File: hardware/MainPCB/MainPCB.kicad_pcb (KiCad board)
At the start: 2 copper layers, 150 x 60 mm, 34 parts, among them J1 USB4125-GF-A, SW1 SW_Push, U1 ESP32-CAM, U2 LSM6DSO32XTR, U3 RASPBERRY_PI_PICO, U4 TIP120

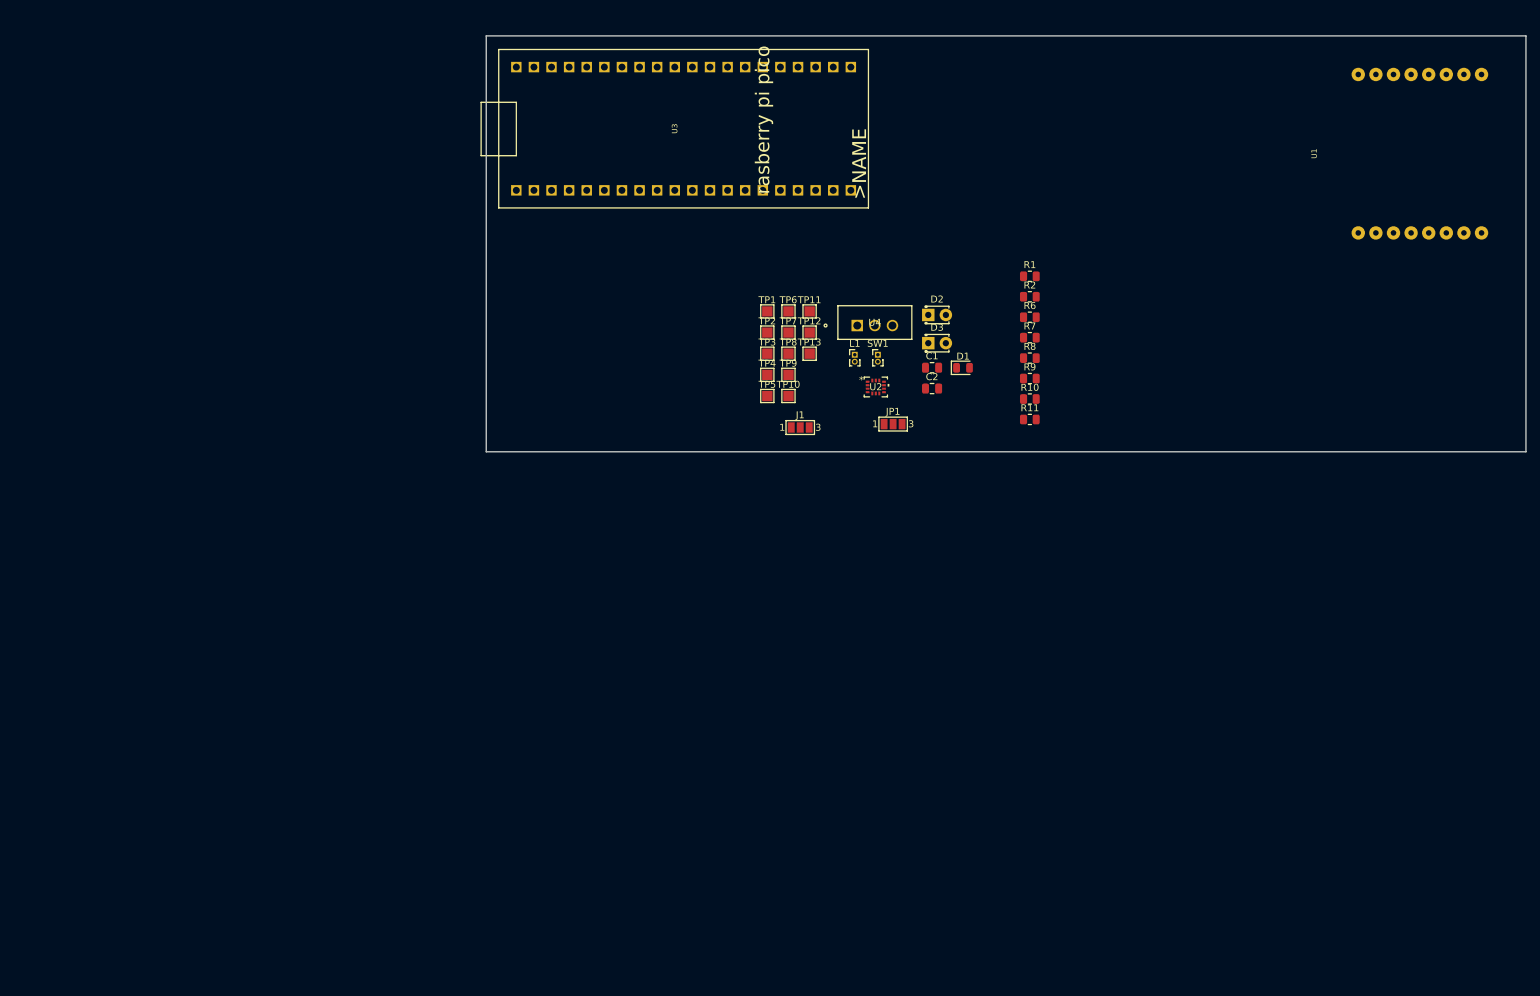
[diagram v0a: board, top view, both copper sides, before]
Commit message: fix: Fixed the LED_GND connecting to GND, also swapped rx and tx on esp32
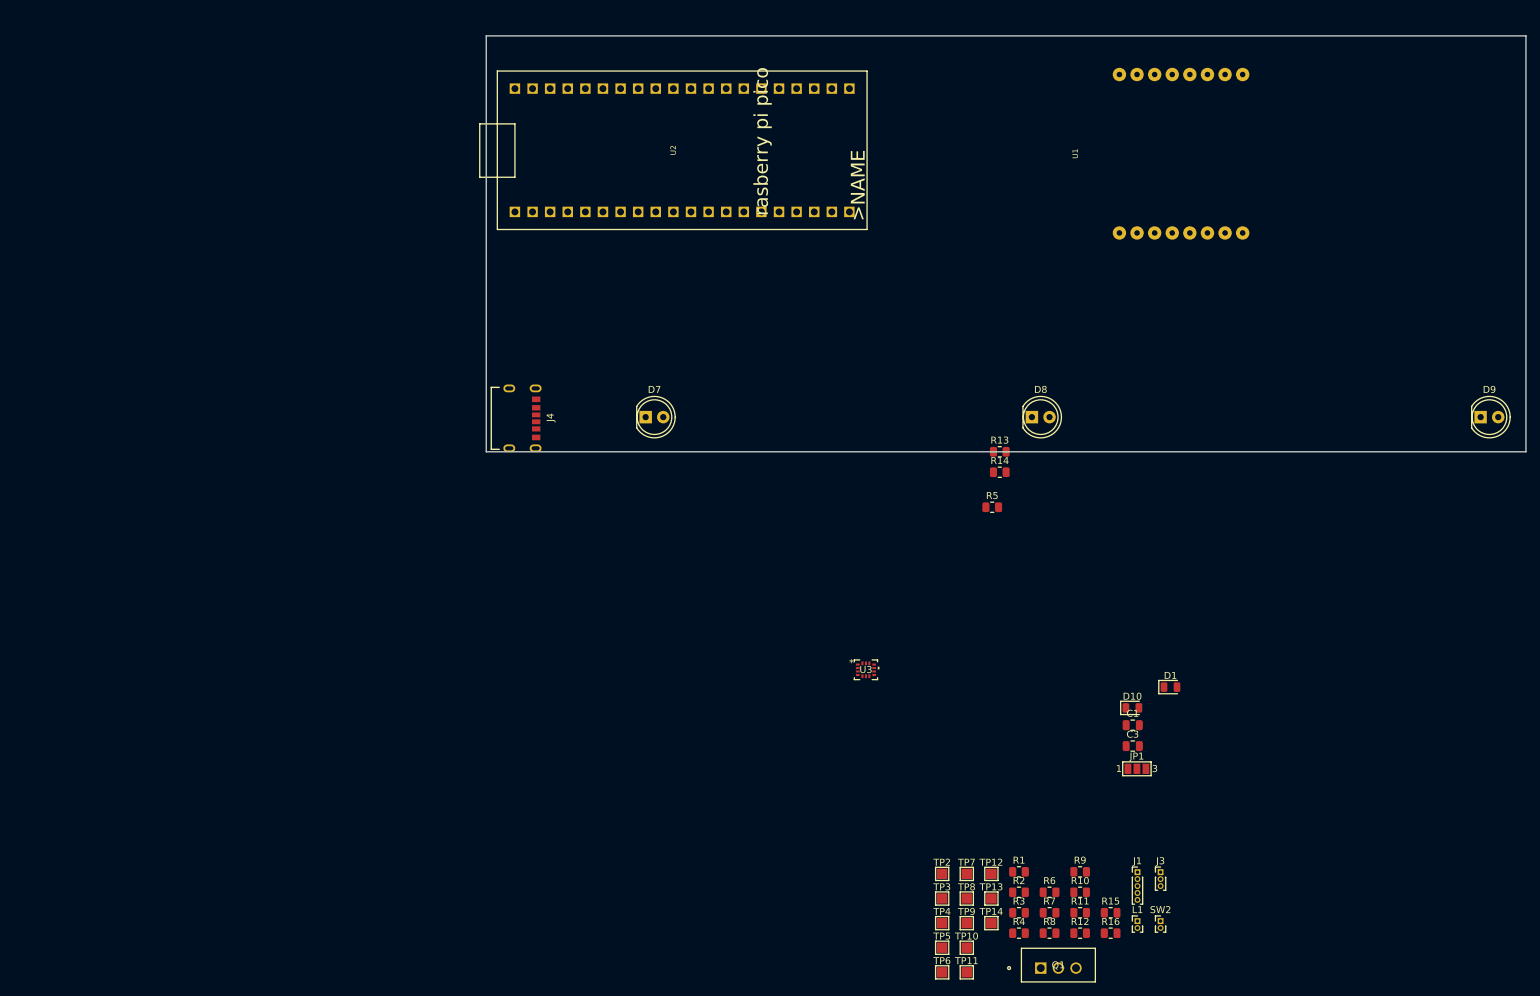
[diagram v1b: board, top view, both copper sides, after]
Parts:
- removed C2: 100nF, Capacitor_SMD:C_0805_2012Metric
- removed D2, D3: Diode, LED_THT:LED_D1.8mm_W3.3mm_H2.4mm
- removed SW1: SW_Push, Connector_PinHeader_1.00mm:PinHeader_1x02_P1.00mm_Vertical
- removed TP1: TestPoint, TestPoint:TestPoint_Pad_1.5x1.5mm
- removed U4: TIP120, Footprints:TO-220_STM
- added C3: 100nF, Capacitor_SMD:C_0805_2012Metric, F.Cu at (143.3, 152.5)
- added D10: Switch Status LED, LED_SMD:LED_0805_2012Metric, F.Cu at (143.2, 146.9)
- added D7: IR LED, LED_THT:LED_D5.0mm, F.Cu at (73.0, 105.0)
- added D8: IR LED, LED_THT:LED_D5.0mm, F.Cu at (128.7, 105.0)
- added D9: IR LED, LED_THT:LED_D5.0mm, F.Cu at (193.5, 105.0)
- added J3: Conn_01x03, Connector_PinHeader_1.00mm:PinHeader_1x03_P1.00mm_Vertical, F.Cu at (147.3, 170.7)
- added J4: USB4125-GF-A_REVA2, Footprints:GCT_USB4125-GF-A_REVA2, F.Cu at (54.1, 105.2)
- added Q1: TIP120, Footprints:TO-220_STM, F.Cu at (130.0, 184.5)
- added R12: 0, Resistor_SMD:R_0805_2012Metric, F.Cu at (135.7, 179.4)
- added R13: 220, Resistor_SMD:R_0805_2012Metric, F.Cu at (124.1, 110.0)
- added R14: 220, Resistor_SMD:R_0805_2012Metric, F.Cu at (124.1, 113.0)
- added R15: 0, Resistor_SMD:R_0805_2012Metric, F.Cu at (140.1, 176.5)
- added R16: 0, Resistor_SMD:R_0805_2012Metric, F.Cu at (140.1, 179.4)
- added R3: 1k, Resistor_SMD:R_0805_2012Metric, F.Cu at (126.9, 176.5)
- added R4: 5.1k, Resistor_SMD:R_0805_2012Metric, F.Cu at (126.9, 179.4)
- added R5: 220, Resistor_SMD:R_0805_2012Metric, F.Cu at (123.0, 118.0)
- added SW2: SW_Push, Connector_PinHeader_1.00mm:PinHeader_1x02_P1.00mm_Vertical, F.Cu at (147.3, 177.7)
- added TP14: Switch_TP, TestPoint:TestPoint_Pad_1.5x1.5mm, F.Cu at (122.9, 178.0)
- D1: value Diode -> 1N4004
- J1: value USB4125-GF-A -> Conn_01x05; footprint Jumper:SolderJumper-3_P1.3mm_Open_Pad1.0x1.5mm_NumberLabels -> Connector_PinHeader_1.00mm:PinHeader_1x05_P1.00mm_Vertical
- L1: value L -> Solenoid
- R10: value 0 -> 1k
- R2: value 1k -> 5.1k
- TP10: value TestPoint -> VUSB_TP
- TP11: value TestPoint -> GND_TP
- TP12: value TestPoint -> 3V3_TP
- TP13: value TestPoint -> MOSI_TP
- TP2: value TestPoint -> Transistor_Base_TP
- TP3: value TestPoint -> Transistor_GND_TP
- TP4: value TestPoint -> MISO_TP
- TP5: value TestPoint -> SDA_TP
- TP6: value TestPoint -> SCL_TP
- TP7: value TestPoint -> CS1_TP
- TP8: value TestPoint -> CS2_TP
- TP9: value TestPoint -> SCK_TP
- U2: value LSM6DSO32XTR -> RASPBERRY_PI_PICO; footprint Footprints:LGA_O32XTR_STM -> Footprints:RASPBERRY_PI_PICO
- U3: value RASPBERRY_PI_PICO -> LSM6DSO32XTR; footprint Footprints:RASPBERRY_PI_PICO -> Footprints:LGA_O32XTR_STM
- moved TP11 98.0 mm to (119.3, 185.1)
- moved TP6 97.9 mm to (115.8, 185.1)
- moved L1 91.3 mm to (144.0, 177.7)
- moved R2 85.9 mm to (126.9, 173.6)
- moved R1 85.9 mm to (126.9, 170.6)
- moved TP10 83.7 mm to (119.3, 181.6)
- moved TP5 83.5 mm to (115.8, 181.6)
- moved TP9 83.2 mm to (119.3, 178.0)
- moved TP4 83.0 mm to (115.8, 178.0)
- moved R6 83.0 mm to (131.3, 173.6)
- moved R7 83.0 mm to (131.3, 176.5)
- moved R8 83.0 mm to (131.3, 179.4)
- moved TP13 82.9 mm to (122.9, 174.4)
- moved U3 82.8 mm to (104.8, 141.4), turned to 0 degrees
- moved TP8 82.7 mm to (119.3, 174.4)
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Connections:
- C1 pad 1: +5V -> 3V3
- C1 pad 2: Net-(U2-Vdd_IO) -> GND
- D1 pad 2: +5V -> VUSB
- J1 pad 1: (no net) -> /PI_IO12
- J1 pad 2: (no net) -> /PI_IO13
- J1 pad 3: (no net) -> /PI_IO13
- L1 pad 2: +5V -> VUSB
- R1 pad 2: Net-(R1-Pad2) -> Net-(Q1-Pad1)
- R10 pad 2: +5V -> GND
- R11 pad 1: Net-(D3-A) -> Net-(R11-Pad1)
- R11 pad 2: +5V -> /CS2
- R2 pad 1: /Switch -> Net-(J4-CC2)
- R2 pad 2: +5V -> GND_LED
- R6 pad 1: Net-(R6-Pad1) -> Net-(U3-SDA)
- R6 pad 2: /SCL -> /SDA
- R7 pad 1: /MOSI -> Net-(U3-SDA)
- R7 pad 2: Net-(U2-SDA) -> /MOSI
- R8 pad 1: /SCL -> Net-(U3-SCL)
- R8 pad 2: Net-(U2-SCL) -> /SCL
- R9 pad 1: /MOSI -> Net-(U3-SCL)
- R9 pad 2: Net-(R9-Pad2) -> /SCK
- TP10 pad 1: /MISO -> VUSB
- TP11 pad 1: /CS1 -> GND
- TP12 pad 1: /MOSI -> 3V3
- TP13 pad 1: /SCL -> /MOSI
- TP2 pad 1: Net-(JP1-C) -> Net-(Q1-Pad1)
- TP4 pad 1: /Switch -> /MISO
- TP5 pad 1: /CS2 -> /SDA
- TP6 pad 1: /MISO -> /SCL
- TP7 pad 1: /Solenoid -> /CS1
- TP8 pad 1: /SCK -> /CS2
- TP9 pad 1: /MOSI -> /SCK
- U1 pad 5V: unconnected-(U1-Pad5V) -> VUSB
- U1 pad IO12: /MISO -> Net-(R15-Pad1)
- U1 pad IO13: /CS2 -> Net-(R11-Pad1)
- U1 pad IO16: Net-(R6-Pad1) -> /SCL
- U1 pad IO2: unconnected-(U1-PadIO2) -> /CAM_IO2
- U1 pad IO4: Net-(R9-Pad2) -> /SDA

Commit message: started on the pcb, arranged components into groups
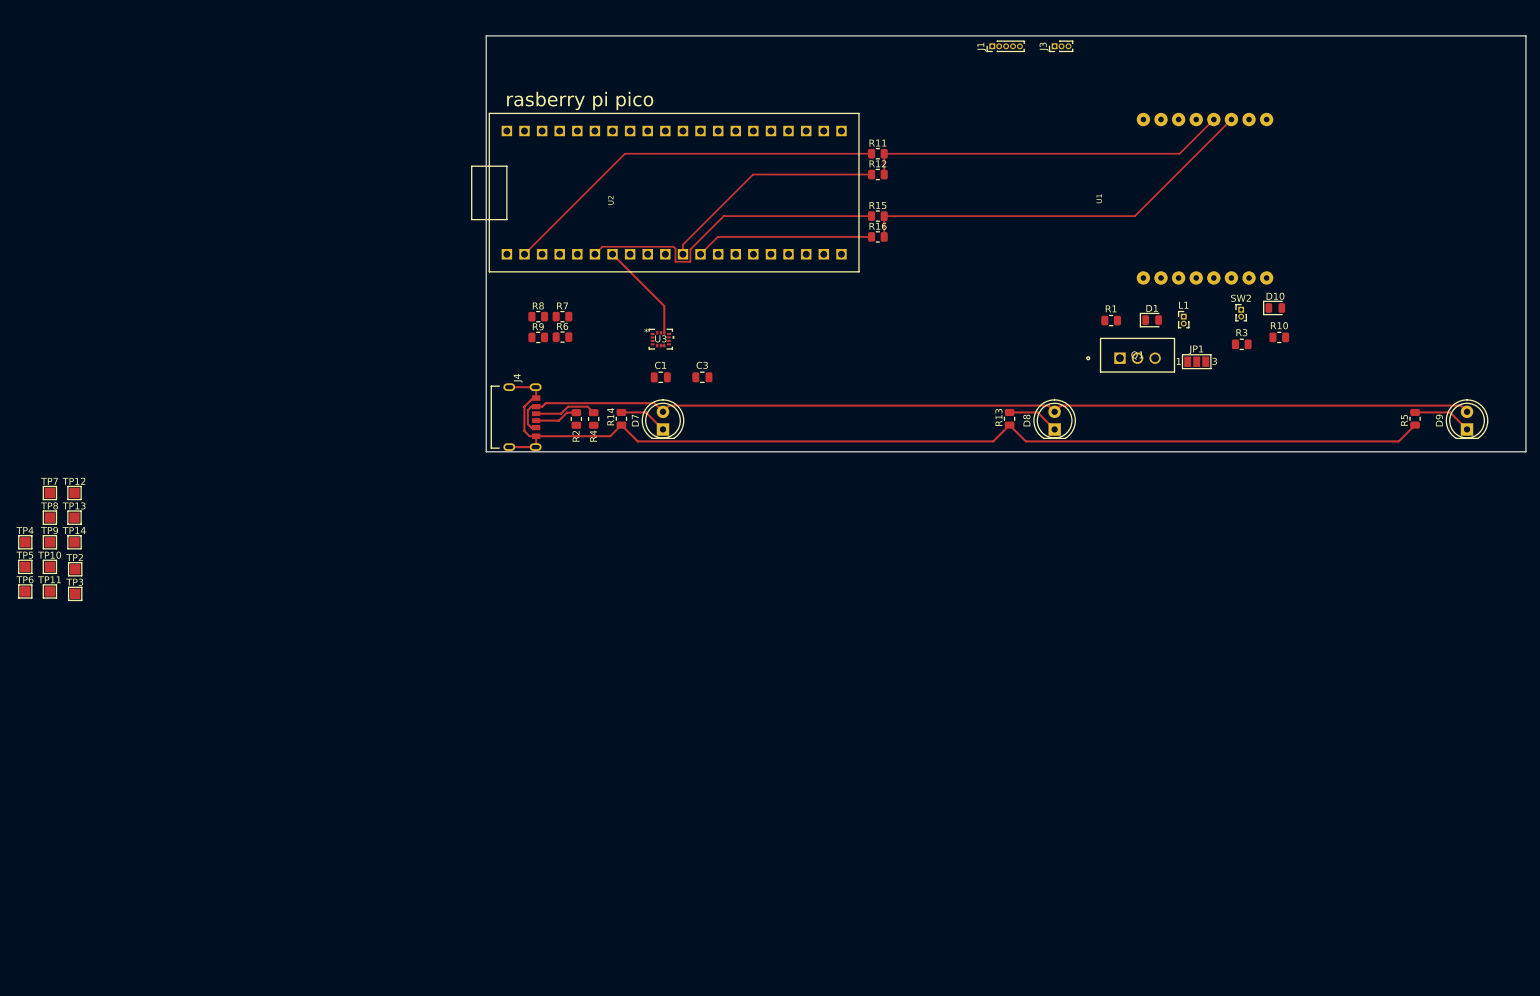
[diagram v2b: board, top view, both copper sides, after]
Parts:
- moved TP10 143.2 mm to (-12.9, 126.6)
- moved TP5 143.2 mm to (-16.5, 126.6)
- moved TP11 143.2 mm to (-12.9, 130.2)
- moved TP12 143.2 mm to (-9.40, 116.0)
- moved TP13 143.2 mm to (-9.40, 119.5)
- moved TP14 143.2 mm to (-9.40, 123.0)
- moved TP4 143.2 mm to (-16.5, 123.0)
- moved TP6 143.2 mm to (-16.5, 130.2)
- moved TP7 143.2 mm to (-12.9, 116.0)
- moved TP8 143.2 mm to (-12.9, 119.5)
- moved TP9 143.2 mm to (-12.9, 123.0)
- moved TP2 132.6 mm to (-9.30, 127.0)
- moved TP3 132.6 mm to (-9.30, 130.5)
- moved J1 121.0 mm to (123.0, 51.5), turned to 90 degrees
- moved J3 120.1 mm to (132.0, 51.5), turned to 90 degrees
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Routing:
- net GND_LED: track 0.00 -> 149.9 mm
- net /VLED: track 0.00 -> 141.3 mm
- net Net-(R15-Pad1): track 0.00 -> 58.9 mm
- net /CS2: track 0.00 -> 56.1 mm
- net Net-(R11-Pad1): track 0.00 -> 52.6 mm
- net /MISO: track 0.00 -> 46.1 mm
- net /UART TX: track 0.00 -> 32.8 mm
- net /UART RX: track 0.00 -> 25.7 mm
- net /CS1: track 0.00 -> 14.4 mm
- net Net-(J4-CC1): track 0.00 -> 9.07 mm
- net Net-(D9-K): track 0.00 -> 8.52 mm
- net Net-(D8-K): track 0.00 -> 7.52 mm
- net Net-(D7-K): track 0.00 -> 7.02 mm
- net Net-(J4-CC2): track 0.00 -> 6.27 mm
- net GND: track 0.00 -> 0.50 mm

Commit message: feat: done the pcb
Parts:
- added J2: Conn_01x02, Connector_PinHeader_1.00mm:PinHeader_1x02_P1.00mm_Vertical, F.Cu at (133.8, 106.2)
- added TP15: VLED_TP, TestPoint:TestPoint_Pad_1.5x1.5mm, B.Cu at (80.3, 105.0)
- added TP16: GND_LED_TP, TestPoint:TestPoint_Pad_1.5x1.5mm, B.Cu at (80.3, 109.2)
- TP10, TP11, TP12, TP13, TP14, TP2, TP3, TP4, TP5, TP6, TP7, TP8, TP9: moved to B.Cu
- moved TP9 145.8 mm to (128.5, 87.5), turned to 180 degrees
- moved TP8 141.9 mm to (125.2, 87.5), turned to 180 degrees
- moved TP3 135.7 mm to (103.5, 55.0), turned to 180 degrees
- moved TP10 130.2 mm to (96.2, 55.8), turned to 180 degrees
- moved TP14 129.9 mm to (103.5, 58.8), turned to 180 degrees
- moved TP2 110.0 mm to (76.0, 57.5), turned to 180 degrees
- moved TP6 99.4 mm to (75.2, 92.0), turned to 180 degrees
- moved TP11 94.8 mm to (75.2, 95.5), turned to 180 degrees
- moved TP7 90.1 mm to (72.5, 87.2), turned to 180 degrees
- moved TP4 86.9 mm to (63.5, 89.0), turned to 180 degrees
- moved TP5 85.7 mm to (60.5, 89.0), turned to 180 degrees
- moved Q1 84.9 mm to (68.6, 52.8), turned to 180 degrees
- moved TP13 77.7 mm to (63.5, 92.8), turned to 180 degrees
- moved J3 77.7 mm to (54.5, 57.1)
- moved JP1 77.0 mm to (86.7, 57.0), turned to 180 degrees
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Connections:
- net /VLED renamed VLED
- J1 pad 3: /PI_IO13 -> /PI_IO14
- J1 pad 4: /PI_IO14 -> /PI_IO15
- R12 pad 2: /UART TX -> /UART RX
- R16 pad 2: /UART RX -> /UART TX
- U2 pad GP14: /PI_IO13 -> /PI_IO14
- U2 pad GP15: /PI_IO14 -> /PI_IO15
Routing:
- net VUSB: track 0.00 -> 111.4 mm, vias 0 -> 3
- net /SDA: track 0.00 -> 86.0 mm, vias 0 -> 3
- net /MOSI: track 0.00 -> 83.2 mm, vias 0 -> 2
- net /SCK: track 0.00 -> 83.2 mm, vias 0 -> 2
- net /SCL: track 0.00 -> 74.5 mm, vias 0 -> 3
- net 3V3: track 0.00 -> 70.8 mm, vias 0 -> 2
- net Net-(R15-Pad1): track 58.9 -> 6.60 mm
- net /CAM_IO2: track 0.00 -> 47.2 mm, vias 0 -> 2
- net Net-(R11-Pad1): track 52.6 -> 6.93 mm
- net GND_LED: track 149.9 -> 110.6 mm, vias 0 -> 1
- net VLED: track 141.3 -> 102.9 mm, vias 0 -> 2
- net Net-(D1-A): track 0.00 -> 31.5 mm
- net /Switch: track 0.00 -> 26.6 mm, vias 0 -> 2
- net /Solenoid: track 0.00 -> 23.7 mm
- net /MISO: track 46.1 -> 67.6 mm, vias 0 -> 2
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- added copper zone on B.Cu, net GND
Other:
- board size 150 x 60 mm -> 100 x 65 mm
